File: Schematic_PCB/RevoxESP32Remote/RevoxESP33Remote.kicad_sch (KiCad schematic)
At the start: 30 parts, among them J1 SerialLink, J2 Conn_01x04, J3 Conn_01x10, J4 Conn_01x05, J5 Conn_01x04, J6 Conn_01x03, J7 Conn_01x03, Q1 BC550, Q2 2N2222, Q3 BC550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

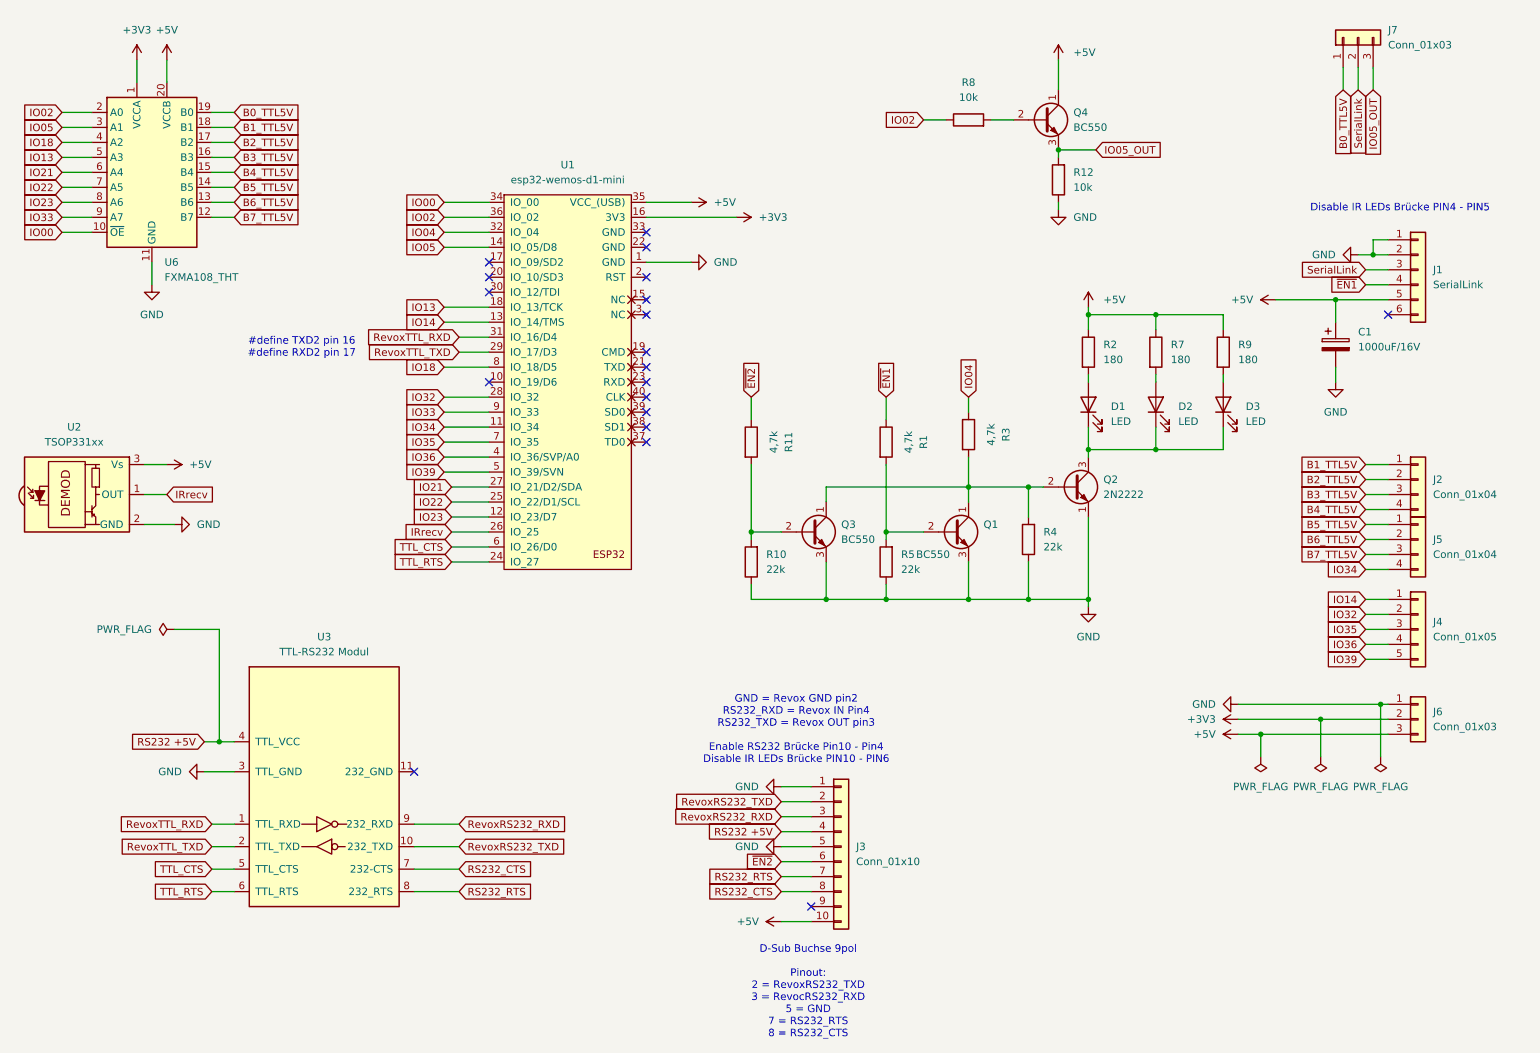
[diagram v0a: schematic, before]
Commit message: sendIR durch sendRevoxFrame ersetzt. Leiterplatte eneuert.
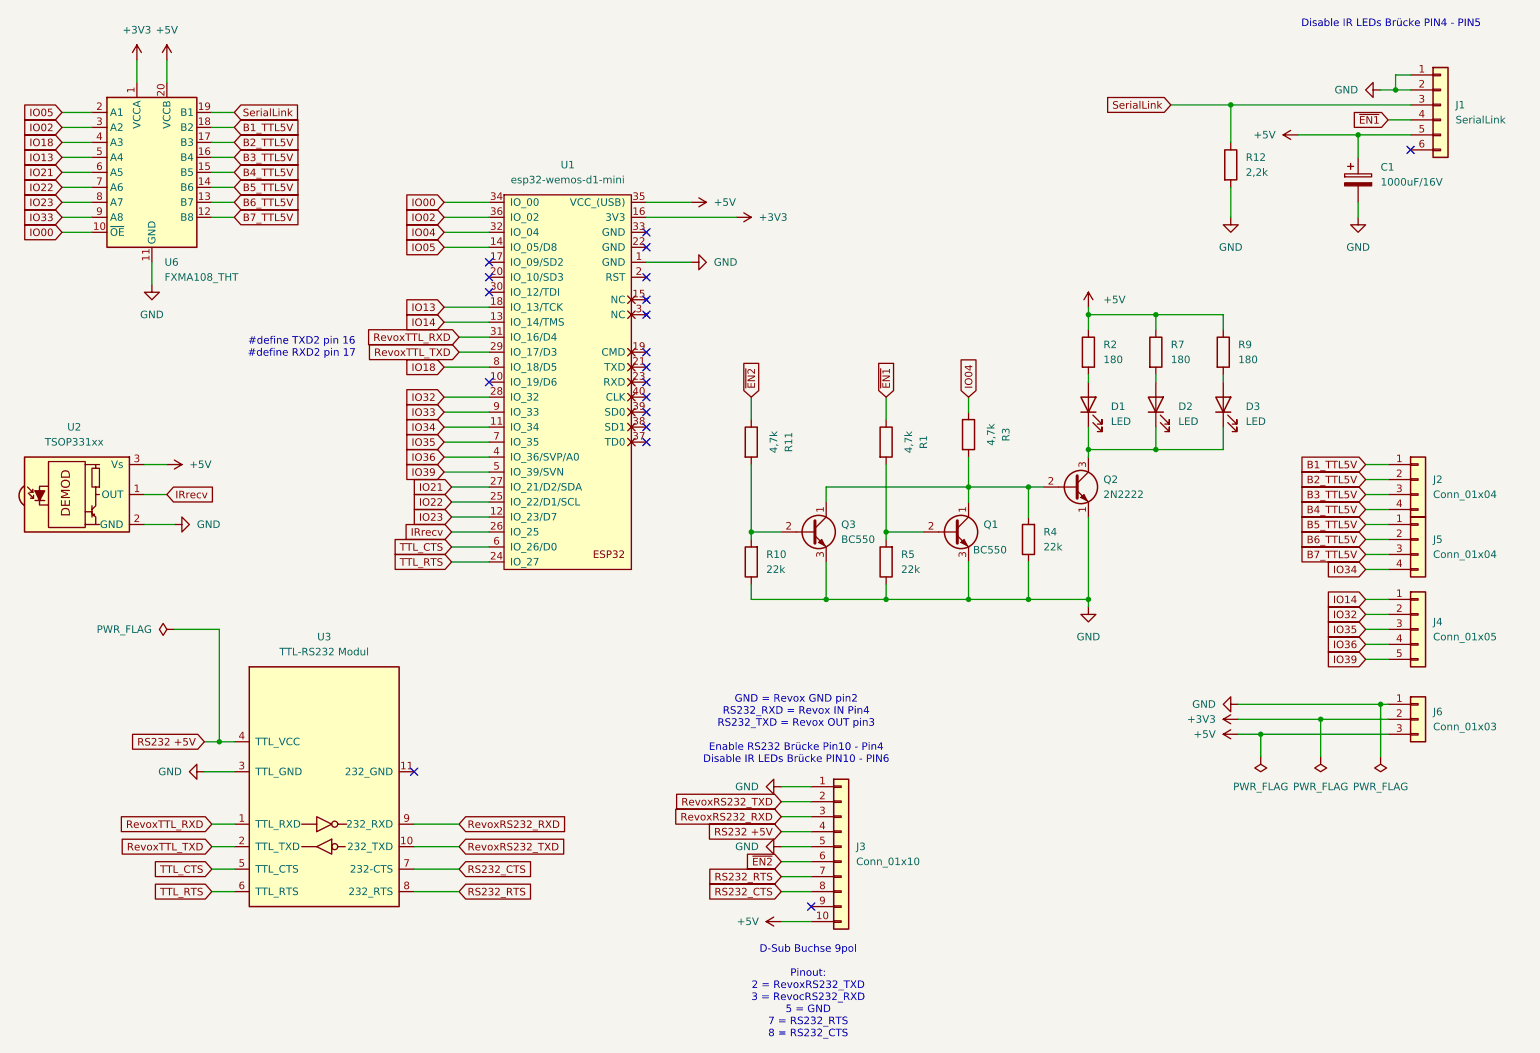
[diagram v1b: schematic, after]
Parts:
- removed J7: Conn_01x03, Connector_PinHeader_2.54mm:PinHeader_1x03_P2.54mm_Vertical, symbol Connector_Generic:Conn_01x03
- removed Q4: BC550, Package_TO_SOT_THT:TO-92_Inline, symbol Transistor_BJT:BC550
- removed R8: 10k, Resistor_THT:R_Axial_DIN0309_L9.0mm_D3.2mm_P12.70mm_Horizontal, symbol Device:R
- R12: value 10k -> 2,2k
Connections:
- net B0_TTL5V is gone; now on net SerialLink: U6.19 (B1)
- net IO05_OUT is gone; now on net GND: R12.2
- net GND: no longer R12.1
- net IO02: now also U6.3 (A2); no longer U6.2 (A0)
- net IO05: now also U6.2 (A1); no longer U6.3 (A1)
- net SerialLink: now also R12.1
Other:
- moved on the sheet: C1, J1

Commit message: Bugfix: Einige verbesserungen im Javascript, 0X wurde nicht korrekt ausgeführt.
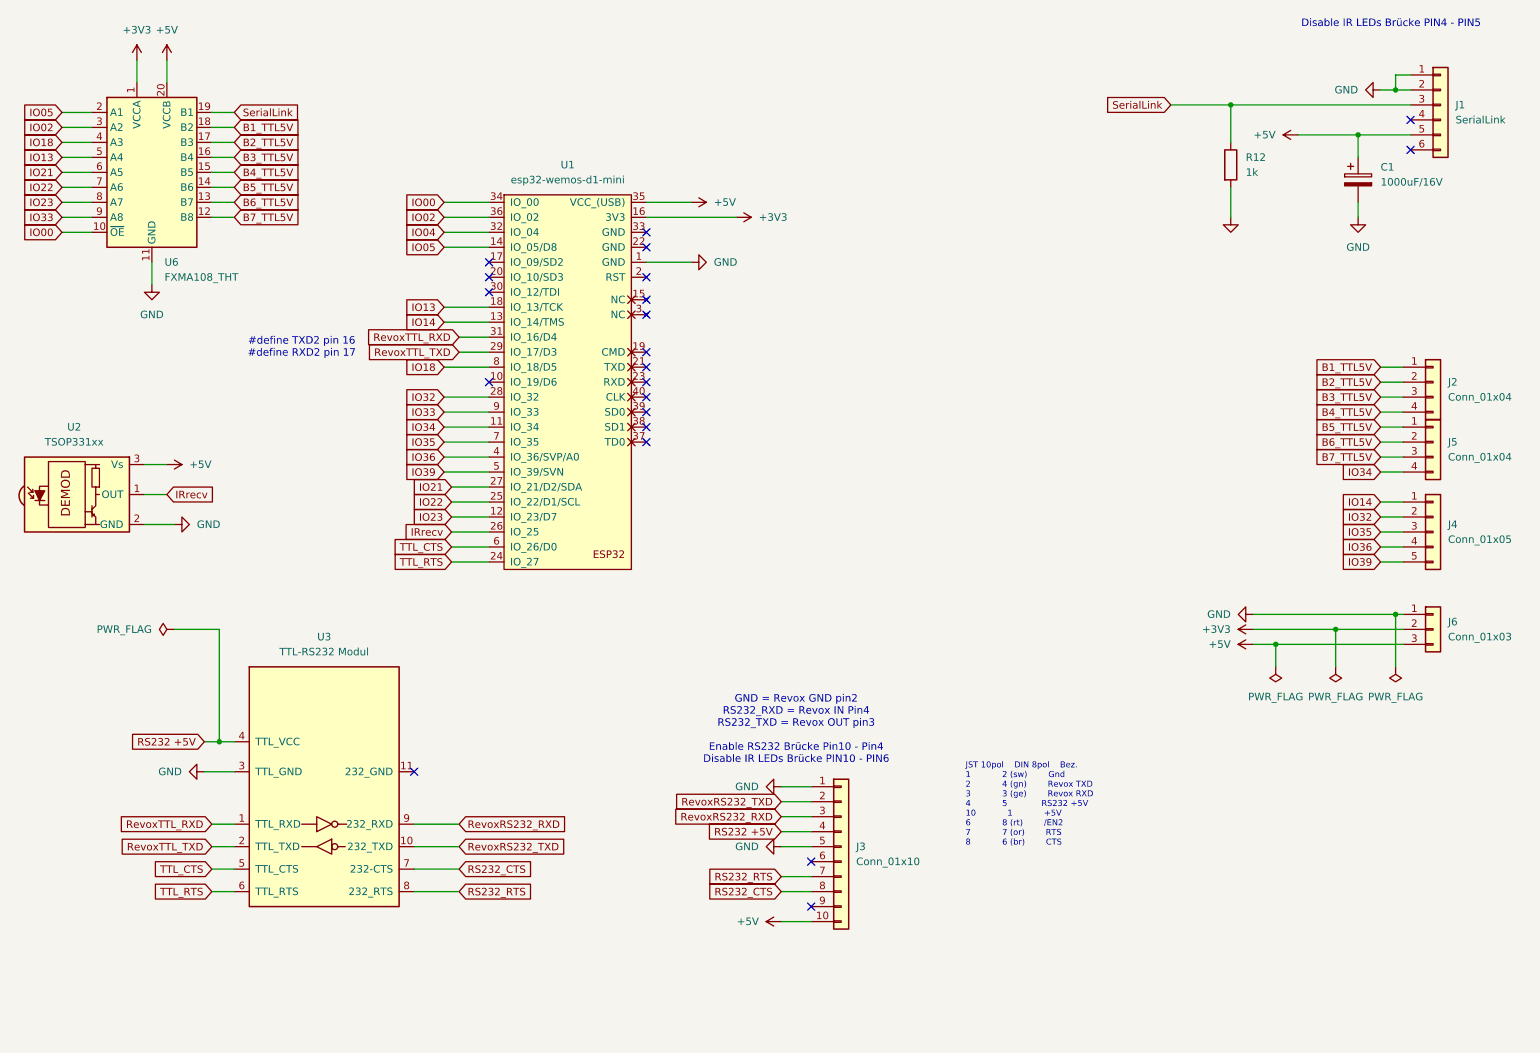
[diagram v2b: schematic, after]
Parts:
- removed D1, D2, D3: LED, LED_THT:LED_D3.0mm_Horizontal_O1.27mm_Z2.0mm_IRBlack, symbol Device:LED
- removed Q1, Q3: BC550, Package_TO_SOT_THT:TO-92_Inline, symbol Transistor_BJT:BC550
- removed Q2: 2N2222, Package_TO_SOT_THT:TO-92_Inline, symbol Transistor_BJT:2N3904
- removed R1, R11, R3: 4,7k, Resistor_THT:R_Axial_DIN0309_L9.0mm_D3.2mm_P12.70mm_Horizontal, symbol Device:R
- removed R10, R4, R5: 22k, Resistor_THT:R_Axial_DIN0309_L9.0mm_D3.2mm_P12.70mm_Horizontal, symbol Device:R
- removed R2, R7, R9: 180, Resistor_THT:R_Axial_DIN0309_L9.0mm_D3.2mm_P12.70mm_Horizontal, symbol Device:R
- R12: value 2,2k -> 1k
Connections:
- net ~{EN1}: no longer names the net of J1.4 (Pin_4)
- net ~{EN2}: no longer names the net of J3.6 (Pin_6)
- no-connect marks 19 -> 21
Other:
- note added: "JST 10pol DIN 8pol Bez. 1 2 (sw) Gnd 2 4 (gn) Revox TXD 3 3 (ge) Revox RXD 4 5 RS232 +5V 10 1 +5V 6 8 (rt) /EN2 7 7 (or) RTS 8 6 (br) CTS"
- note removed: "D-Sub Buchse 9pol Pinout: 2 = RevoxRS232_TXD 3 = RevocRS232_RXD 5 = GND 7 = RS232_RTS 8 = RS232_CTS"
- moved on the sheet: J2, J4, J5, J6

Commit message: Light Sleep Mode hinzugefügt.
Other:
- note added: "JST 10pol DIN 8pol Bez. Farbe Vbl. 1 2 (sw) Gnd sw 2 4 (rt) Revox TXD gn 3 3 (ws) Revox RXD ge 4 5 (ge) RS232 +5V 10 1 (br) +5V rt 7 7 (bl) RTS or 8 6 (vio) CTS br"
- note added: "JST 6pol. DIN 6pol. 1 (sw) 1 (gnd) 2 (br) 2 (gnd) 3 (ge) 3 (SerialLink) 4 (bl) 4 (nc) 5 (rt) 5 (+5V) 6 (vio) 6 (nc)"
- note added: "Lötseite"
- note removed: "JST 10pol DIN 8pol Bez. 1 2 (sw) Gnd 2 4 (gn) Revox TXD 3 3 (ge) Revox RXD 4 5 RS232 +5V 10 1 +5V 6 8 (rt) /EN2 7 7 (or) RTS 8 6 (br) CTS"
